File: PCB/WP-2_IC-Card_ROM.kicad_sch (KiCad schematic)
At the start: 5 parts, among them J1 Conn_01x38_Female, U1 29F020

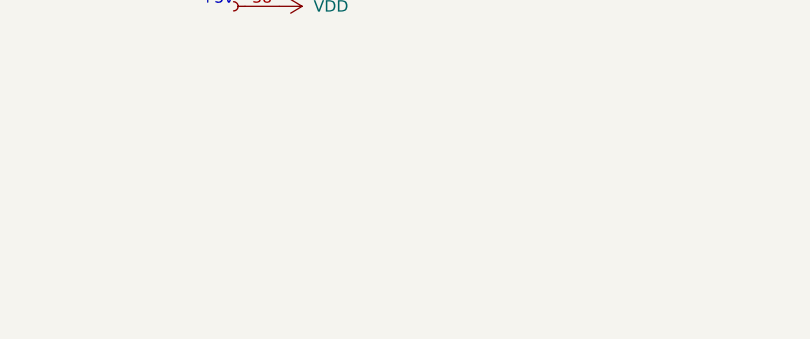
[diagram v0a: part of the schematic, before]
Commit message: local symbol & footprint library organization, add shielded mram version
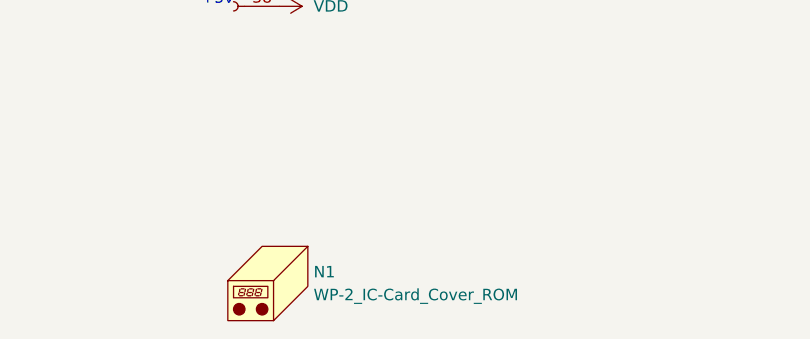
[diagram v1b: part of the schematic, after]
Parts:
- added N1: WP-2_IC-Card_Cover_ROM, 000_LOCAL:WP-2_IC_Card_Cover_ROM, symbol 000_LOCAL:Housing
- C1: footprint 0_LOCAL:C_0805_1mm -> 000_LOCAL:C_0805_1mm; symbol 0_LOCAL:C_Small -> 000_LOCAL:C_Small
- J1: footprint 0_LOCAL:SMS-138-01-x-x_edge -> 000_LOCAL:SMS-138-01-x-x_edge; symbol 0_LOCAL:Conn_01x38_Female -> 000_LOCAL:Conn_01x38_Female
- JP1: footprint 0_LOCAL:JP2_tight -> 000_LOCAL:JP2_tight; symbol 0_LOCAL:Jumper_NO_Small -> 000_LOCAL:Jumper_NO_Small
- R1: footprint 0_LOCAL:R_0805 -> 000_LOCAL:R_0805; symbol 0_LOCAL:R -> 000_LOCAL:R
- U1: footprint 0_LOCAL:TSOP32-dual -> 000_LOCAL:TSOP32-dual; symbol 0_LOCAL:SST39SF020_TSOP -> 000_LOCAL:SST39SF020_TSOP
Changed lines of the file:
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@@
 	)
 	(symbol
-		(lib_id "0_LOCAL:Conn_01x38_Female")
+		(lib_id "000_LOCAL:Conn_01x38_Female")
 		(at 83.82 99.06 0)
 		(mirror y)
@@
 			)
 		)
-		(property "Footprint" "0_LOCAL:SMS-138-01-x-x_edge"
+		(property "Footprint" "000_LOCAL:SMS-138-01-x-x_edge"
 			(at 83.82 99.06 0)
 			(effects
@@
 	)
 	(symbol
-		(lib_id "0_LOCAL:R")
+		(lib_id "000_LOCAL:R")
 		(at 139.7 133.35 0)
 		(unit 1)
@@
 			)
 		)
-		(property "Footprint" "0_LOCAL:R_0805"
+		(property "Footprint" "000_LOCAL:R_0805"
 			(at 137.922 133.35 90)
 			(effects
@@
 	)
 	(symbol
-		(lib_id "0_LOCAL:Jumper_NO_Small")
+		(lib_id "000_LOCAL:Jumper_NO_Small")
 		(at 124.46 139.7 0)
 		(unit 1)
@@
 			)
 		)
-		(property "Footprint" "0_LOCAL:JP2_tight"
+		(property "Footprint" "000_LOCAL:JP2_tight"
 			(at 124.46 139.7 0)
 			(effects
@@
 	)
 	(symbol
-		(lib_id "0_LOCAL:SST39SF020_TSOP")
+		(lib_id "000_LOCAL:SST39SF020_TSOP")
 		(at 193.04 116.84 0)
 		(unit 1)
@@
 			)
 		)
-		(property "Footprint" "0_LOCAL:TSOP32-dual"
+		(property "Footprint" "000_LOCAL:TSOP32-dual"
 			(at 180.34 87.63 0)
 			(effects
@@
 	)
 	(symbol
-		(lib_id "0_LOCAL:C_Small")
+		(lib_id "000_LOCAL:Housing")
+		(at 88.9 177.8 0)
+		(unit 1)
+		(exclude_from_sim yes)
+		(in_bom yes)
+		(on_board yes)
+		(dnp no)
+		(fields_autoplaced yes)
+		(property "Reference" "N1"
+			(at 92.71 176.8474 0)
+			(effects
+				(font
+					(size 1.27 1.27)
+				)
+				(justify left)
+			)
+		)
+		(property "Value" "WP-2_IC-Card_Cover_ROM"
+			(at 92.71 179.3874 0)
+			(effects
+				(font
+					(size 1.27 1.27)
+				)
+				(justify left)
+			)
+		)
+		(property "Footprint" "000_LOCAL:WP-2_IC_Card_Cover_ROM"
+			(at 90.17 176.53 0)
+			(effects
+				(font
+					(size 1.27 1.27)
+				)
+				(hide yes)
+			)
+		)
+		(property "Datasheet" "~"
+			(at 90.17 176.53 0)
+			(effects
+				(font
+					(size 1.27 1.27)
+				)
+				(hide yes)
+			)
+		)
+		(property "Description" "Housing"
+			(at 88.9 177.8 0)
+			(effects
+				(font
+					(size 1.27 1.27)
+				)
+				(hide yes)
+			)
+		)
+		(instances
+			(project ""
+				(path "/f291f000-461a-4127-8876-c8e21ea67ede"
+					(reference "N1")
+					(unit 1)
+				)
+			)
+		)
+	)
+	(symbol
+		(lib_id "000_LOCAL:C_Small")
 		(at 156.21 83.82 180)
 		(unit 1)
@@
 			)
 		)
-		(property "Footprint" "0_LOCAL:C_0805_1mm"
+		(property "Footprint" "000_LOCAL:C_0805_1mm"
 			(at 156.21 83.82 0)
 			(effects

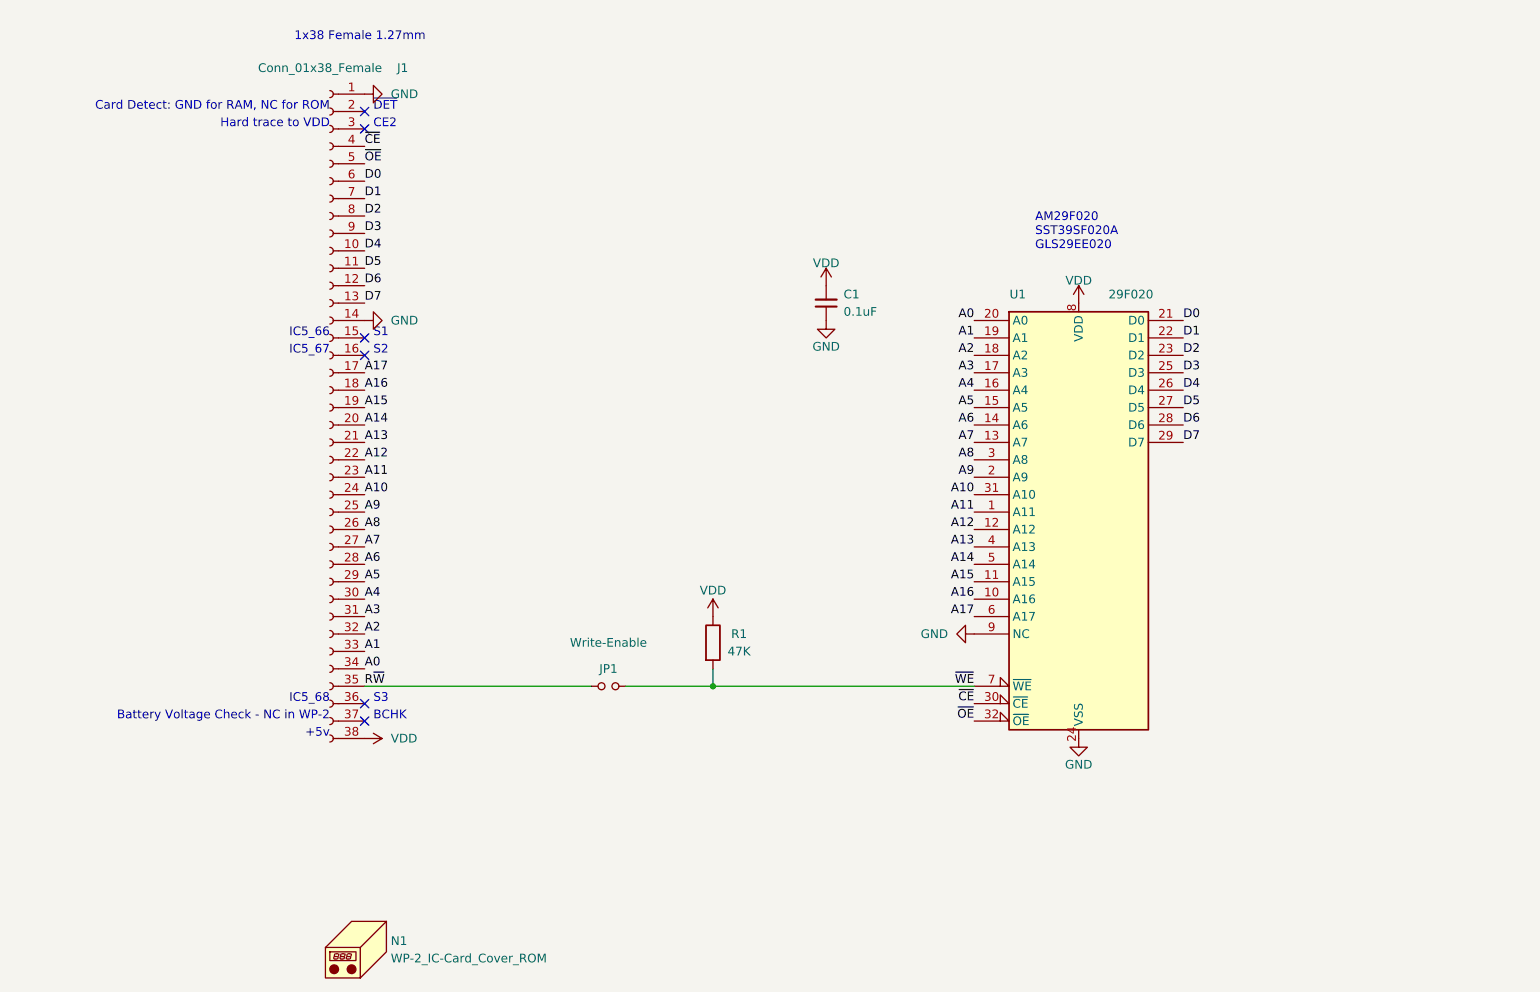
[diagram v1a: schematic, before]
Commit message: cleanup names, cover inside corner reliefs
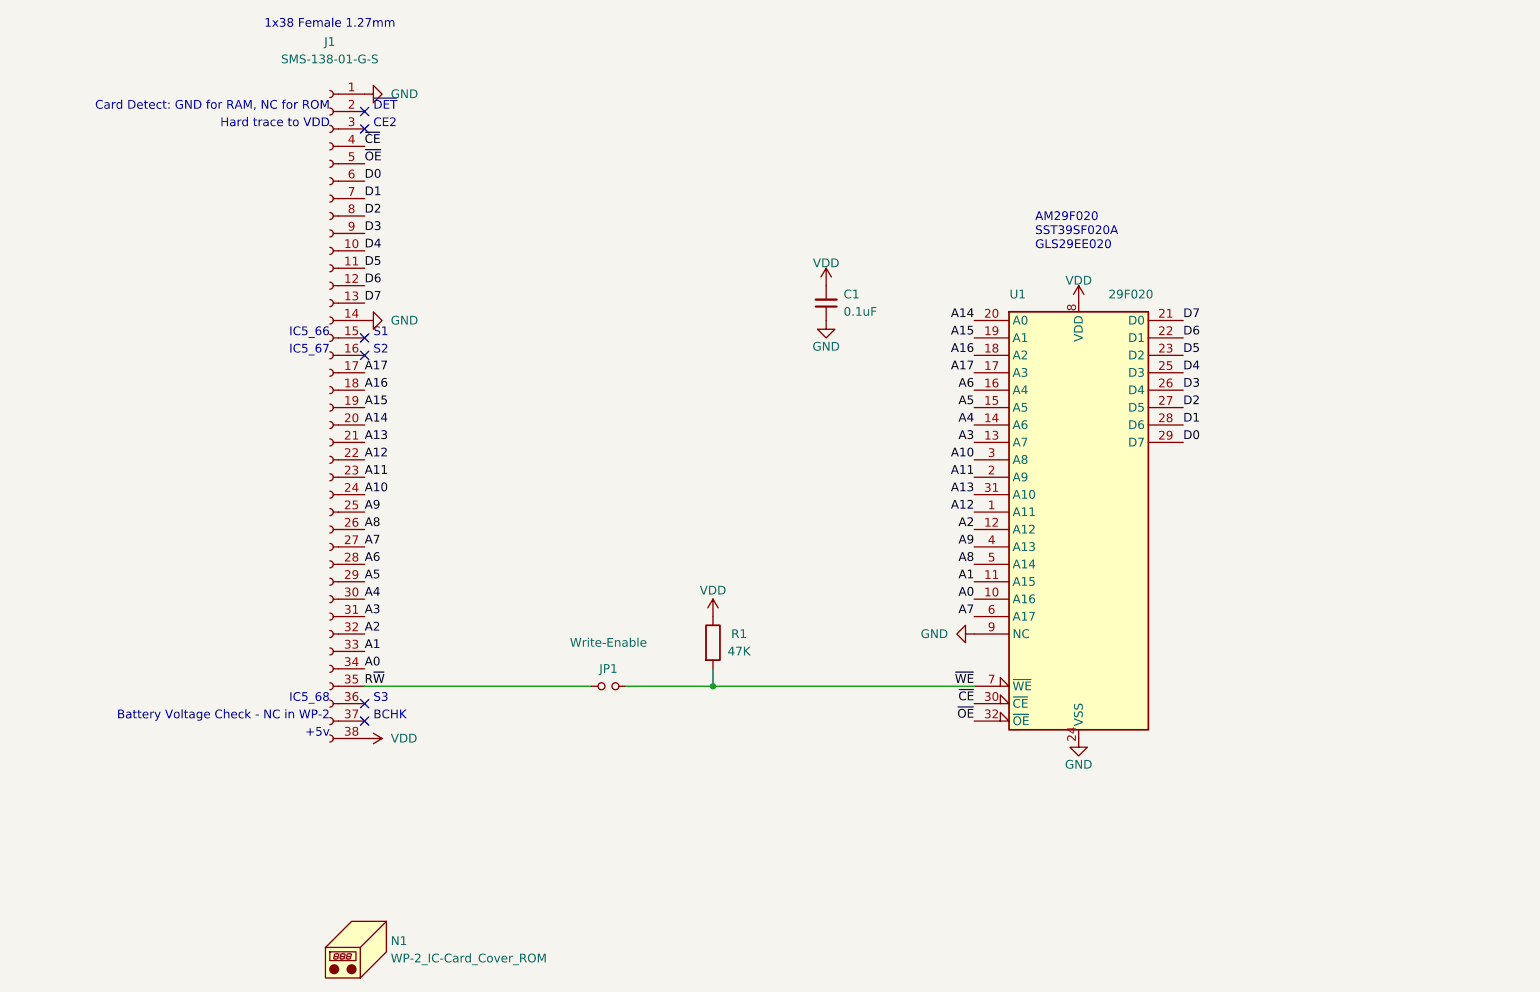
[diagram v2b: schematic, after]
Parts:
- J1: value Conn_01x38_Female -> SMS-138-01-G-S; footprint 000_LOCAL:SMS-138-01-x-x_edge -> 000_LOCAL:SMS-138-01-x-x_pcb_edge; MPN (none) -> SMS-138-01-G-S
- N1: footprint 000_LOCAL:WP-2_IC_Card_Cover_ROM -> 000_LOCAL:WP-2_IC-Card_Cover_ROM
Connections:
- net A0: now also U1.10 (A16); no longer U1.20 (A0)
- net A1: now also U1.11 (A15); no longer U1.19 (A1)
- net A10: now also U1.3 (A8); no longer U1.31 (A10)
- net A11: now also U1.2 (A9); no longer U1.1 (A11)
- net A12: now also U1.1 (A11); no longer U1.12 (A12)
- net A13: now also U1.31 (A10); no longer U1.4 (A13)
- net A14: now also U1.20 (A0); no longer U1.5 (A14)
- net A15: now also U1.19 (A1); no longer U1.11 (A15)
- net A16: now also U1.18 (A2); no longer U1.10 (A16)
- net A17: now also U1.17 (A3); no longer U1.6 (A17)
- net A2: now also U1.12 (A12); no longer U1.18 (A2)
- net A3: now also U1.13 (A7); no longer U1.17 (A3)
- net A4: now also U1.14 (A6); no longer U1.16 (A4)
- net A6: now also U1.16 (A4); no longer U1.14 (A6)
- net A7: now also U1.6 (A17); no longer U1.13 (A7)
- net A8: now also U1.5 (A14); no longer U1.3 (A8)
- net A9: now also U1.4 (A13); no longer U1.2 (A9)
- net D0: now also U1.29 (D7); no longer U1.21 (D0)
- net D1: now also U1.28 (D6); no longer U1.22 (D1)
- net D2: now also U1.27 (D5); no longer U1.23 (D2)
- net D3: now also U1.26 (D4); no longer U1.25 (D3)
- net D4: now also U1.25 (D3); no longer U1.26 (D4)
- net D5: now also U1.23 (D2); no longer U1.27 (D5)
- net D6: now also U1.22 (D1); no longer U1.28 (D6)
- net D7: now also U1.21 (D0); no longer U1.29 (D7)
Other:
- title: TANDY WP-2 256K ROM IC Card -> TANDY WP-2 IC-Card ROM
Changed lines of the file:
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@@
 	(paper "USLetter")
 	(title_block
-		(title "TANDY WP-2 256K ROM IC Card")
-		(date "2023-01-01")
-		(rev "005")
+		(title "TANDY WP-2 IC-Card ROM")
+		(date "2024-10-04")
+		(rev "006")
 		(company "Brian K. White - b.kenyon.w@gmail.com")
+		(comment 1 "github.com/bkw777/WP-2_IC-Card")
 	)
 	(junction
@@
 	(text "1x38 Female 1.27mm"
 		(exclude_from_sim no)
-		(at 97.79 45.72 0)
-		(effects
-			(font
-				(size 1.27 1.27)
-			)
-			(justify right bottom)
+		(at 83.82 43.18 0)
+		(effects
+			(font
+				(size 1.27 1.27)
+			)
 		)
 	)
@@
 	)
 	(label "A14"
-		(at 177.8 121.92 180)
+		(at 177.8 86.36 180)
 		(fields_autoplaced yes)
 		(effects
@@
 	)
 	(label "A16"
-		(at 177.8 127 180)
+		(at 177.8 91.44 180)
 		(fields_autoplaced yes)
 		(effects
@@
 	)
 	(label "D5"
-		(at 208.28 99.06 0)
+		(at 208.28 91.44 0)
 		(fields_autoplaced yes)
 		(effects
@@
 	)
 	(label "D3"
-		(at 208.28 93.98 0)
+		(at 208.28 96.52 0)
 		(fields_autoplaced yes)
 		(effects
@@
 	)
 	(label "A8"
-		(at 177.8 106.68 180)
+		(at 177.8 121.92 180)
 		(fields_autoplaced yes)
 		(effects
@@
 	)
 	(label "D2"
-		(at 208.28 91.44 0)
+		(at 208.28 99.06 0)
 		(fields_autoplaced yes)
 		(effects
@@
 	)
 	(label "A6"
-		(at 177.8 101.6 180)
+		(at 177.8 96.52 180)
 		(fields_autoplaced yes)
 		(effects
@@
 	)
 	(label "A7"
-		(at 177.8 104.14 180)
+		(at 177.8 129.54 180)
 		(fields_autoplaced yes)
 		(effects
@@
 	)
 	(label "A15"
-		(at 177.8 124.46 180)
+		(at 177.8 88.9 180)
 		(fields_autoplaced yes)
 		(effects
@@
 	)
 	(label "A10"
-		(at 177.8 111.76 180)
+		(at 177.8 106.68 180)
 		(fields_autoplaced yes)
 		(effects
@@
 	)
 	(label "A17"
-		(at 177.8 129.54 180)
+		(at 177.8 93.98 180)
 		(fields_autoplaced yes)
 		(effects
@@
 	)
 	(label "D0"
-		(at 208.28 86.36 0)
+		(at 208.28 104.14 0)
 		(fields_autoplaced yes)
 		(effects
@@
 	)
 	(label "A3"
-		(at 177.8 93.98 180)
+		(at 177.8 104.14 180)
 		(fields_autoplaced yes)
 		(effects
@@
 	)
 	(label "A13"
-		(at 177.8 119.38 180)
+		(at 177.8 111.76 180)
 		(fields_autoplaced yes)
 		(effects
@@
 	)
 	(label "D6"
-		(at 208.28 101.6 0)
+		(at 208.28 88.9 0)
 		(fields_autoplaced yes)
 		(effects
@@
 	)
 	(label "A0"
-		(at 177.8 86.36 180)
+		(at 177.8 127 180)
 		(fields_autoplaced yes)
 		(effects
@@
 	)
 	(label "D7"
-		(at 208.28 104.14 0)
+		(at 208.28 86.36 0)
 		(fields_autoplaced yes)
 		(effects
@@
 	)
 	(label "D4"
-		(at 208.28 96.52 0)
+		(at 208.28 93.98 0)
 		(fields_autoplaced yes)
 		(effects
@@
 	)
 	(label "A12"
-		(at 177.8 116.84 180)
+		(at 177.8 114.3 180)
 		(fields_autoplaced yes)
 		(effects
@@
 	)
 	(label "A2"
-		(at 177.8 91.44 180)
+		(at 177.8 116.84 180)
 		(fields_autoplaced yes)
 		(effects
@@
 	)
 	(label "D1"
-		(at 208.28 88.9 0)
+		(at 208.28 101.6 0)
 		(fields_autoplaced yes)
 		(effects
@@
 	)
 	(label "A11"
-		(at 177.8 114.3 180)
+		(at 177.8 109.22 180)
 		(fields_autoplaced yes)
 		(effects
@@
 	)
 	(label "A4"
-		(at 177.8 96.52 180)
+		(at 177.8 101.6 180)
 		(fields_autoplaced yes)
 		(effects
@@
 	)
 	(label "A1"
-		(at 177.8 88.9 180)
+		(at 177.8 124.46 180)
 		(fields_autoplaced yes)
 		(effects
@@
 	)
 	(label "A9"
-		(at 177.8 109.22 180)
+		(at 177.8 119.38 180)
 		(fields_autoplaced yes)
 		(effects
@@
 		(dnp no)
 		(property "Reference" "J1"
-			(at 95.25 49.53 0)
-			(effects
-				(font
-					(size 1.27 1.27)
-				)
-				(justify left)
-			)
-		)
-		(property "Value" "Conn_01x38_Female"
-			(at 91.44 49.53 0)
-			(effects
-				(font
-					(size 1.27 1.27)
-				)
-				(justify left)
-			)
-		)
-		(property "Footprint" "000_LOCAL:SMS-138-01-x-x_edge"
+			(at 83.82 45.72 0)
+			(effects
+				(font
+					(size 1.27 1.27)
+				)
+			)
+		)
+		(property "Value" "SMS-138-01-G-S"
+			(at 83.82 48.26 0)
+			(effects
+				(font
+					(size 1.27 1.27)
+				)
+			)
+		)
+		(property "Footprint" "000_LOCAL:SMS-138-01-x-x_pcb_edge"
 			(at 83.82 99.06 0)
 			(effects
@@
 		)
 		(property "Description" ""
+			(at 83.82 99.06 0)
+			(effects
+				(font
+					(size 1.27 1.27)
+				)
+				(hide yes)
+			)
+		)
+		(property "MPN" "SMS-138-01-G-S"
 			(at 83.82 99.06 0)
 			(effects
@@
 			)
 		)
-		(property "Footprint" "000_LOCAL:WP-2_IC_Card_Cover_ROM"
+		(property "Footprint" "000_LOCAL:WP-2_IC-Card_Cover_ROM"
 			(at 90.17 176.53 0)
 			(effects

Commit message: rom name & revision
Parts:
- N1: now left out of the parts list
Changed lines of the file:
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@@
 		(unit 1)
 		(exclude_from_sim yes)
-		(in_bom yes)
+		(in_bom no)
 		(on_board yes)
 		(dnp no)

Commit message: rom wren sw, boms, footprints, shielded mram
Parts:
- removed U1: 29F020, 000_LOCAL:TSOP32-dual, symbol 000_LOCAL:SST39SF020_TSOP
- added U1: 29F0x0_TSOP, 000_LOCAL:TSOP32-dual, symbol 000_LOCAL:29F0x0_TSOP
- C1: value 0.1uF -> 1u; footprint 000_LOCAL:C_0805_1mm -> 000_LOCAL:C_0805; MPN (none) -> CL21A105KBCLNNC
- R1: value 47K -> 47k; MPN (none) -> RMCF0805JT47K0
- SW1: renamed from JP1; footprint 000_LOCAL:JP2_tight -> 000_LOCAL:CUS-12TB pth; symbol 000_LOCAL:Jumper_NO_Small -> 000_LOCAL:SW_SPDT_CUS-12; MPN (none) -> EG1215AA
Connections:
- net A0: now also U1.10 (A16)
- net A1: now also U1.11 (A15)
- net A10: now also U1.3 (A8)
- net A11: now also U1.2 (A9)
- net A12: now also U1.1 (A11)
- net A13: now also U1.31 (A10)
- net A14: now also U1.20 (A0)
- net A15: now also U1.19 (A1)
- net A16: now also U1.18 (A2)
- net A17: now also U1.17 (A3)
- net A2: now also U1.12 (A12)
- net A3: now also U1.13 (A7)
- net A4: now also U1.14 (A6)
- net A5: now also U1.15 (A5)
- net A6: now also U1.16 (A4)
- net A7: now also U1.6 (A17)
- net A8: now also U1.5 (A14)
- net A9: now also U1.4 (A13)
- net D0: now also U1.29 (D7)
- net D1: now also U1.28 (D6)
- net D2: now also U1.27 (D5)
- net D3: now also U1.26 (D4)
- net D4: now also U1.25 (D3)
- net D5: now also U1.23 (D2)
- net D6: now also U1.22 (D1)
- net D7: now also U1.21 (D0)
- net GND: now also SW1.S, U1.24 (VSS), U1.9 (A18)
- net R~{W}: now also SW1.2 (C); no longer SW1.1
- net ~{CE}: now also U1.30 (~{CE})
- net ~{OE}: now also U1.32 (~{OE})
- net ~{WE}: now also SW1.1, U1.7 (~{WE}); no longer SW1.2
- net VDD renamed VCC
- net VCC: now also U1.8 (VCC)
- no-connect marks 6 -> 7
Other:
- note added: "1.2mm thick or less"
- note added: "C&K SK-12C0405-SG 1.5 RT E-Switch EG1215AA Nidec CUS-12TB Alps Alpine SSSS811101"
- note added: "Compatible with up to 512k chip but only up to 256k is used. x = 1,2,4 -> 128k,256k,512k AM29F0x0 SST39SF0x0A GLS29EE0x0 AT29C0x0A MX29F0x0C"
- note removed: "AM29F020 SST39SF020A GLS29EE020"
- title: TANDY WP-2 IC-Card ROM -> WP-2_IC-Card_ROM
